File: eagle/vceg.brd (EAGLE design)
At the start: 100 x 80 mm, 65 parts, among them IC1 4052N, IC2 4001N, IC3 TL074P, IC5 CA3080E, Q1 2N3906INLINE, Q2 2N3906INLINE, U1 POWER

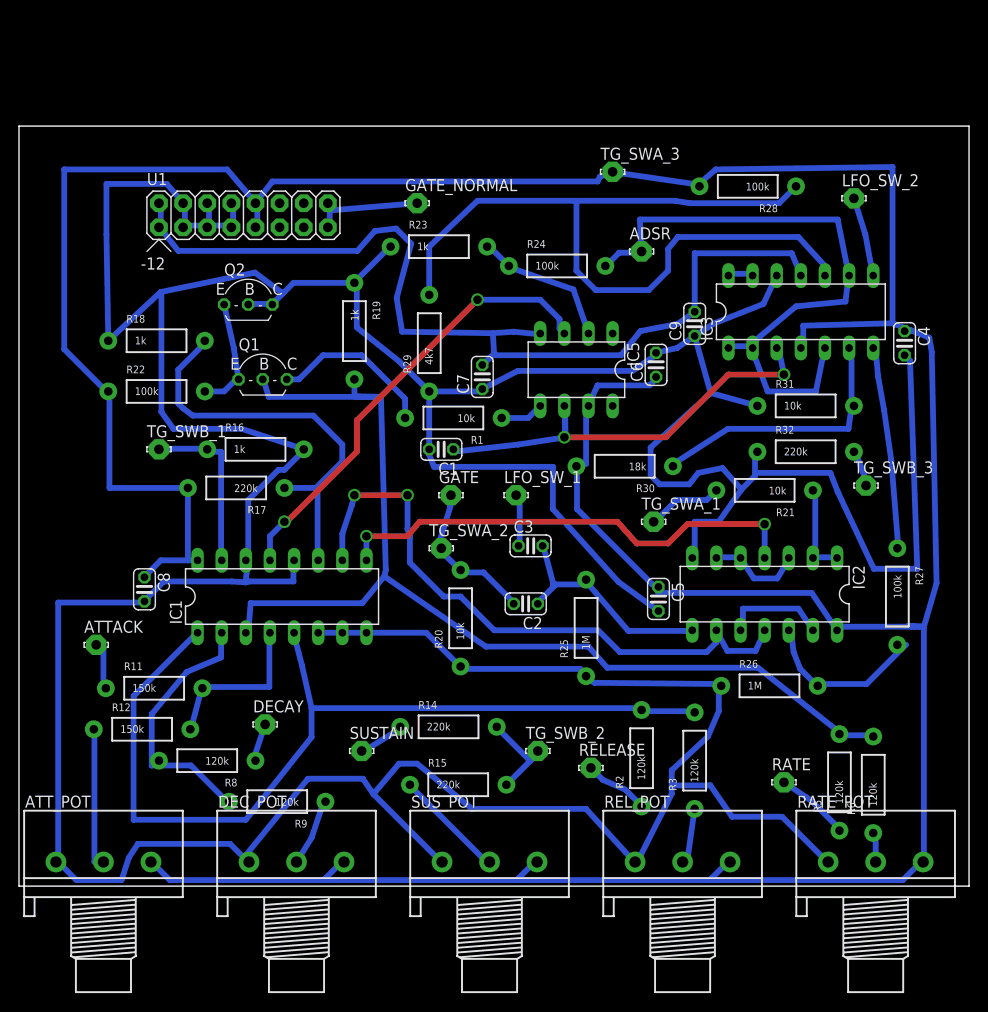
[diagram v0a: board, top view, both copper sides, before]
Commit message: lm13700 subbed and offset mixer added
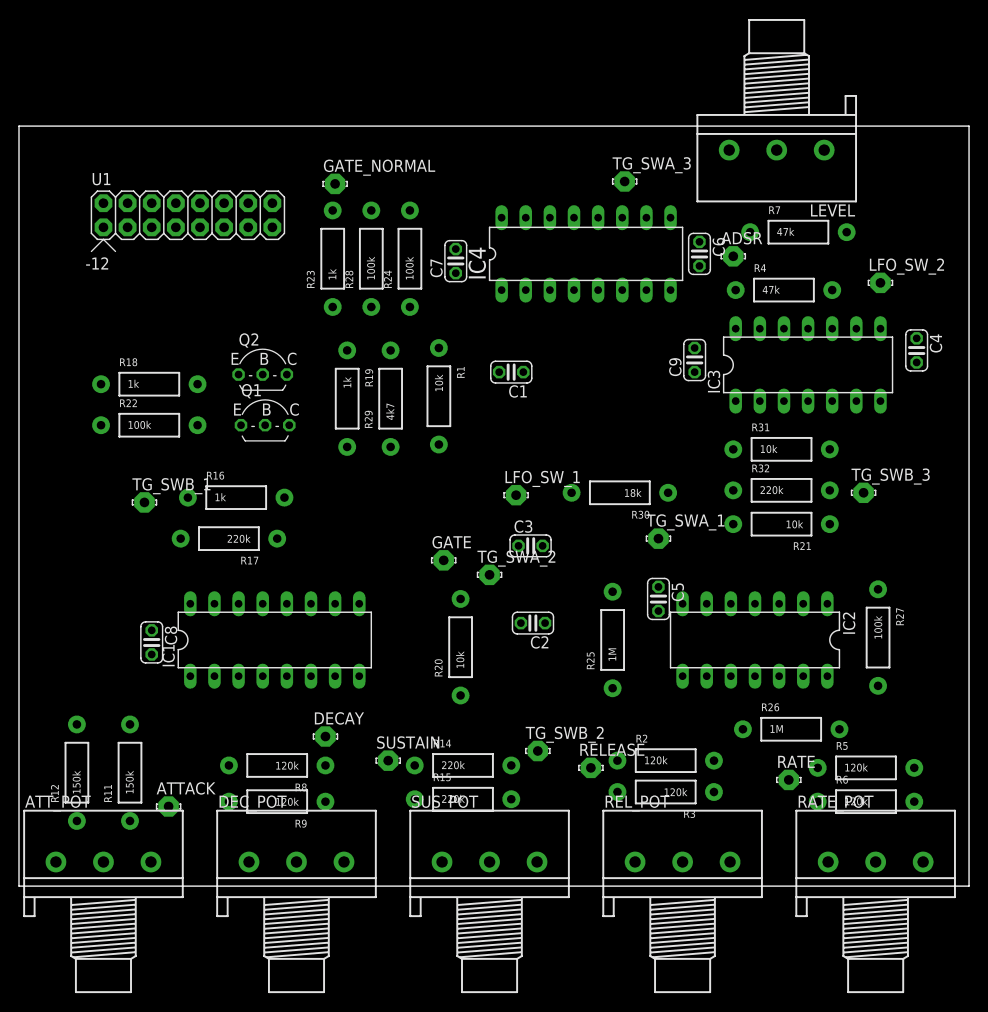
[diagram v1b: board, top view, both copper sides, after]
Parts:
- removed IC5: CA3080E, ota:DIL08
- added IC4: LM13700N, synthdiy:DIL16
- added LEVEL: 50k, pot:3RP/1610N
- added R4, R7: 47k, SparkFun-Resistors:AXIAL-0.4
- moved R28 40.4 mm to (37.1, 66.0), turned to 90 degrees
- moved ATTACK 18.6 mm to (15.7, 8.38)
- moved R24 15.5 mm to (41.1, 66.0), turned to 90 degrees
- moved C6 12.5 mm to (71.6, 66.5), turned to 270 degrees
- moved C7 12.5 mm to (46.0, 65.8)
- moved R23 11.2 mm to (33.0, 66.0), turned to 90 degrees
- moved C1 11.0 mm to (51.8, 54.1)
- moved ADSR 9.67 mm to (75.2, 66.3)
- moved LFO_SW_2 9.32 mm to (90.7, 63.5)
- moved R11 9.25 mm to (11.7, 11.9), turned to 90 degrees
- moved GATE_NORMAL 8.87 mm to (33.3, 73.9)
- moved R12 8.24 mm to (6.10, 11.9), turned to 90 degrees
- moved Q2 7.52 mm to (25.7, 53.8)
- moved R8 7.38 mm to (27.2, 12.7)
- moved R19 7.15 mm to (34.5, 51.3)
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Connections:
- new net N$42: ADSR.MP, IC3.14, R4.P$1
- new net N$43: IC3.13, R4.P$2, R7.P$1
- net +12V: now also IC4.11; no longer IC5.7
- net -12V: now also IC4.10, IC4.13, IC4.14, IC4.15, IC4.16, IC4.6; no longer IC5.4
- net GND: now also IC4.7, LEVEL.1; no longer IC3.12
- net N$24: now also IC4.4; no longer IC5.2
- net N$26: now also LEVEL.3, R7.P$2; no longer ADSR.MP
- net N$28: now also IC4.5; no longer IC5.6
- net N$39: now also IC4.1; no longer IC5.5
- net N$40: now also IC3.12, LEVEL.2; no longer IC3.13, IC3.14
- net N$41: now also IC4.3; no longer IC5.3
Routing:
- net GND: track 545.1 -> 0.00 mm
- net +12V: track 398.6 -> 0.00 mm
- net N$5: track 113.6 -> 0.00 mm
- net -12V: track 101.8 -> 0.00 mm
- net N$2: track 97.3 -> 0.00 mm
- net N$34: track 86.8 -> 0.00 mm
- net N$26: track 66.6 -> 0.00 mm
- net N$17: track 65.4 -> 0.00 mm, vias 2 -> 0
- net N$20: track 50.6 -> 0.00 mm, vias 2 -> 0
- net N$41: track 47.8 -> 0.00 mm, vias 2 -> 0
- net N$28: track 47.6 -> 0.00 mm, vias 2 -> 0
- net N$16: track 43.7 -> 0.00 mm
- net N$33: track 28.8 -> 0.00 mm
- net N$8: track 28.4 -> 0.00 mm
- net N$25: track 24.8 -> 0.00 mm
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
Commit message: layout for lm13700 and offset amp
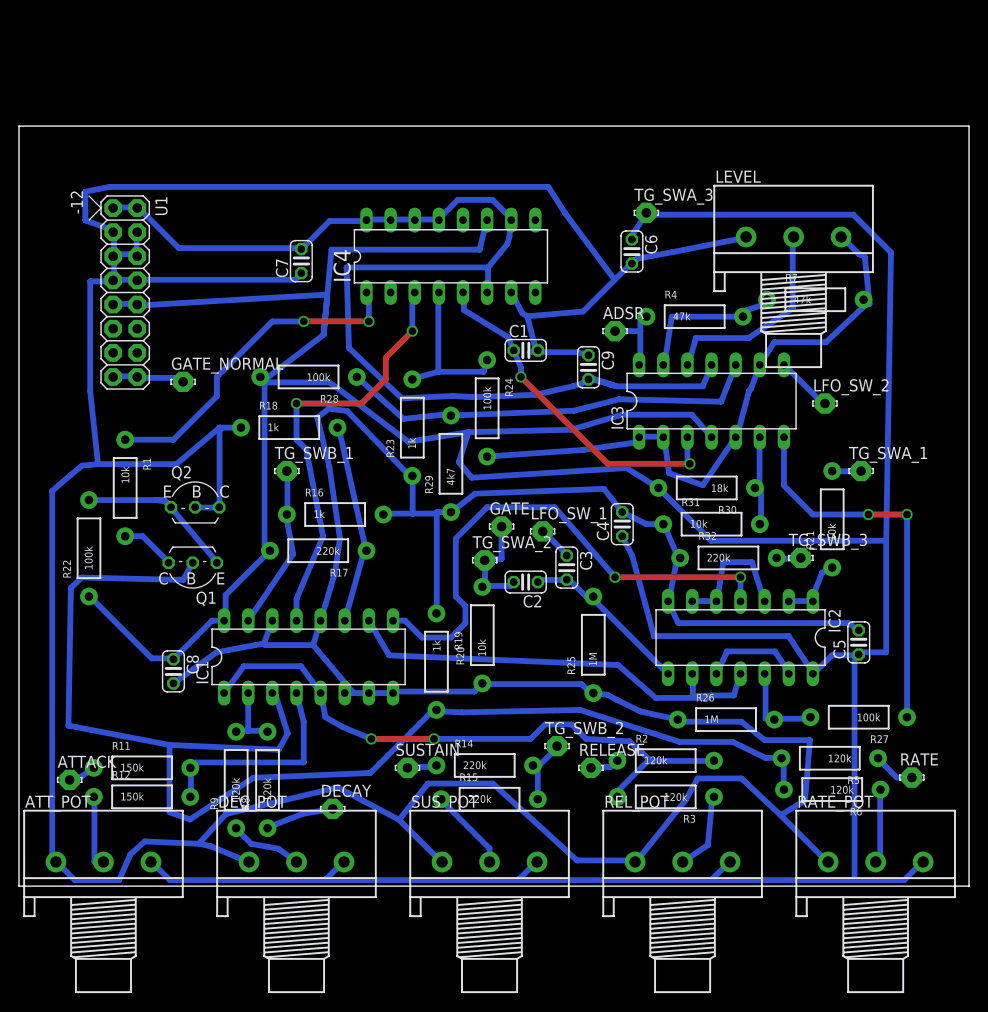
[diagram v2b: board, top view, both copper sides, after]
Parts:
- moved C4 36.0 mm to (63.5, 38.1), turned to 90 degrees
- moved R1 34.4 mm to (11.2, 41.9)
- moved R19 29.2 mm to (43.9, 23.6)
- moved GATE_NORMAL 26.3 mm to (17.3, 53.1)
- moved TG_SWA_1 22.5 mm to (88.6, 43.7)
- moved C5 21.6 mm to (88.4, 25.7), turned to 90 degrees
- moved R23 19.7 mm to (41.4, 48.3)
- moved R24 17.7 mm to (49.3, 50.3), turned to 270 degrees
- moved Q1 16.4 mm to (18.3, 34.0), turned to 180 degrees
- moved C7 16.3 mm to (29.7, 65.8)
- moved Q2 15.7 mm to (18.5, 39.9)
- moved R18 15.4 mm to (28.4, 48.3)
- moved TG_SWB_1 15.3 mm to (28.2, 43.7)
- moved ADSR 14.7 mm to (62.7, 58.4)
- moved R22 14.4 mm to (7.37, 35.6), turned to 90 degrees
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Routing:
- net GND: track 0.00 -> 544.5 mm
- net +12V: track 0.00 -> 439.8 mm
- net N$5: track 0.00 -> 138.0 mm
- net -12V: track 0.00 -> 124.2 mm
- net N$2: track 0.00 -> 64.5 mm, vias 0 -> 2
- net N$26: track 0.00 -> 64.5 mm
- net N$20: track 0.00 -> 55.6 mm, vias 0 -> 2
- net N$17: track 0.00 -> 49.9 mm
- net N$41: track 0.00 -> 44.9 mm, vias 0 -> 2
- net N$34: track 0.00 -> 44.4 mm
- net N$29: track 0.00 -> 40.6 mm, vias 0 -> 2
- net N$28: track 0.00 -> 36.3 mm, vias 0 -> 2
- net N$39: track 0.00 -> 35.2 mm, vias 0 -> 2
- net N$11: track 0.00 -> 23.4 mm
- net N$40: track 0.00 -> 21.7 mm
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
